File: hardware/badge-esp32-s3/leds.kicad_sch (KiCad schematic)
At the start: 2 parts

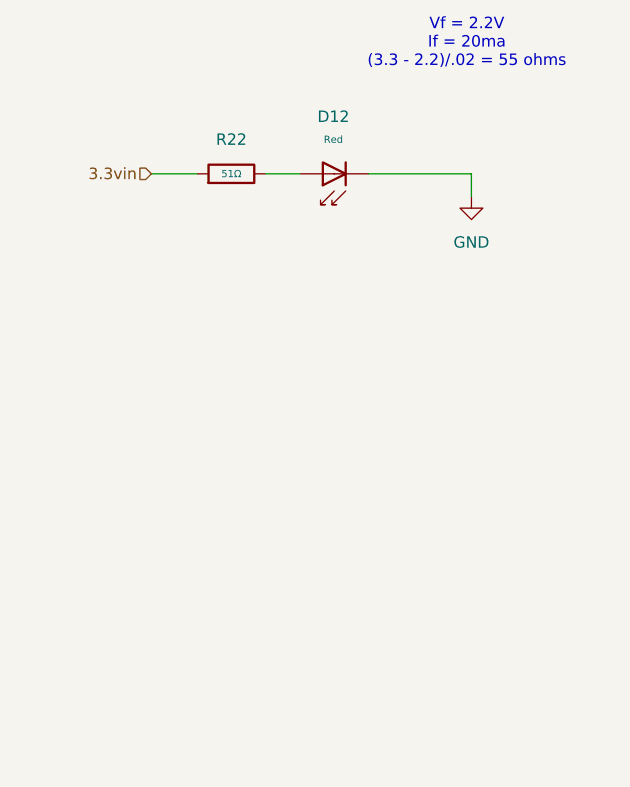
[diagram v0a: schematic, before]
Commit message: Add new tri-color LED, library update
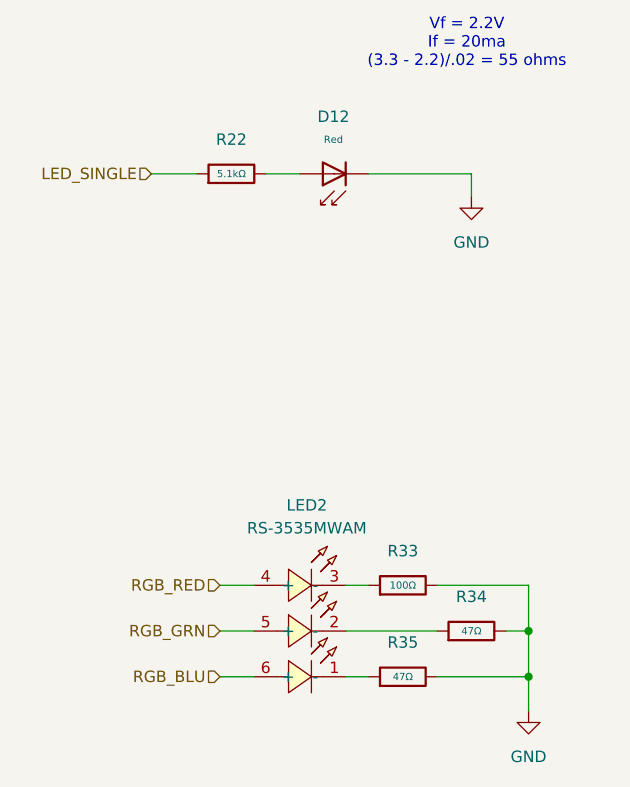
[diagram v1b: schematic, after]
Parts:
- removed R22: 51Ω, PCM_JLCPCB:R_0603, symbol PCM_JLCPCB-Resistors:0603,51Ω
- added LED2: RS-3535MWAM, lcsc-lib:LED-ARRAY-SMD_L3.7-W3.5-P1.10-TL, symbol lcsc-lib:RS-3535MWAM
- added R22: 5.1kΩ, PCM_JLCPCB:R_0402, symbol PCM_JLCPCB-Resistors:0402,5.1kΩ
- added R33: 100Ω, PCM_JLCPCB:R_0402, symbol PCM_JLCPCB-Resistors:0402,100Ω
- added R34, R35: 47Ω, PCM_JLCPCB:R_0402, symbol PCM_JLCPCB-Resistors:0402,47Ω
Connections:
- net GND: now also R33.2, R34.2, R35.2
- net at D12.2: now also R22.2
- new net: LED2.1 (-), R35.1
- new net: LED2.2 (-), R34.1
- new net: LED2.3 (-), R33.1
- new net LED_SINGLE: R22.1
- new net RGB_BLU: LED2.6 (+)
- new net RGB_GRN: LED2.5 (+)
- new net RGB_RED: LED2.4 (+)

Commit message: Annotate schematic
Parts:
- renumbered D12 to D10, LED2 to LED1, R22 to R19, R33 to R20, R35 to R21, R34 to R22
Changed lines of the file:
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@@
 		(dnp no)
 		(fields_autoplaced yes)
-		(property "Reference" "D12"
+		(property "Reference" "D10"
 			(at 135.7947 93.98 90)
 			(effects
@@
 			(project ""
 				(path "/e2af9a6c-dbe9-4de2-9ba6-ea213a7300ec/cf4b41f4-37f8-453c-b748-b2fe0c3fb5a0"
-					(reference "D12")
+					(reference "D10")
 					(unit 1)
 				)
@@
 		(dnp no)
 		(fields_autoplaced yes)
-		(property "Reference" "LED2"
+		(property "Reference" "LED1"
 			(at 132.84 137.16 0)
 			(effects
@@
 			(project ""
 				(path "/e2af9a6c-dbe9-4de2-9ba6-ea213a7300ec/cf4b41f4-37f8-453c-b748-b2fe0c3fb5a0"
-					(reference "LED2")
+					(reference "LED1")
 					(unit 1)
 				)
@@
 		(dnp no)
 		(fields_autoplaced yes)
-		(property "Reference" "R33"
+		(property "Reference" "R20"
 			(at 143.51 142.24 90)
 			(effects
@@
 			(project ""
 				(path "/e2af9a6c-dbe9-4de2-9ba6-ea213a7300ec/cf4b41f4-37f8-453c-b748-b2fe0c3fb5a0"
-					(reference "R33")
+					(reference "R20")
 					(unit 1)
 				)
@@
 		(dnp no)
 		(fields_autoplaced yes)
-		(property "Reference" "R35"
+		(property "Reference" "R21"
 			(at 143.51 152.4 90)
 			(effects
@@
 			(project ""
 				(path "/e2af9a6c-dbe9-4de2-9ba6-ea213a7300ec/cf4b41f4-37f8-453c-b748-b2fe0c3fb5a0"
-					(reference "R35")
+					(reference "R21")
 					(unit 1)
 				)
@@
 		(dnp no)
 		(fields_autoplaced yes)
-		(property "Reference" "#PWR035"
+		(property "Reference" "#PWR032"
 			(at 151.13 109.22 0)
 			(effects
@@
 			(project ""
 				(path "/e2af9a6c-dbe9-4de2-9ba6-ea213a7300ec/cf4b41f4-37f8-453c-b748-b2fe0c3fb5a0"
-					(reference "#PWR035")
+					(reference "#PWR032")
 					(unit 1)
 				)
@@
 		(dnp no)
 		(fields_autoplaced yes)
-		(property "Reference" "#PWR016"
+		(property "Reference" "#PWR033"
 			(at 157.48 166.37 0)
 			(effects
@@
 			(project ""
 				(path "/e2af9a6c-dbe9-4de2-9ba6-ea213a7300ec/cf4b41f4-37f8-453c-b748-b2fe0c3fb5a0"
-					(reference "#PWR016")
+					(reference "#PWR033")
 					(unit 1)
 				)
@@
 		(dnp no)
 		(fields_autoplaced yes)
-		(property "Reference" "R22"
+		(property "Reference" "R19"
 			(at 124.46 96.52 90)
 			(effects
@@
 			(project ""
 				(path "/e2af9a6c-dbe9-4de2-9ba6-ea213a7300ec/cf4b41f4-37f8-453c-b748-b2fe0c3fb5a0"
-					(reference "R22")
+					(reference "R19")
 					(unit 1)
 				)
@@
 		(dnp no)
 		(fields_autoplaced yes)
-		(property "Reference" "R34"
+		(property "Reference" "R22"
 			(at 151.13 147.32 90)
 			(effects
@@
 			(project ""
 				(path "/e2af9a6c-dbe9-4de2-9ba6-ea213a7300ec/cf4b41f4-37f8-453c-b748-b2fe0c3fb5a0"
-					(reference "R34")
+					(reference "R22")
 					(unit 1)
 				)

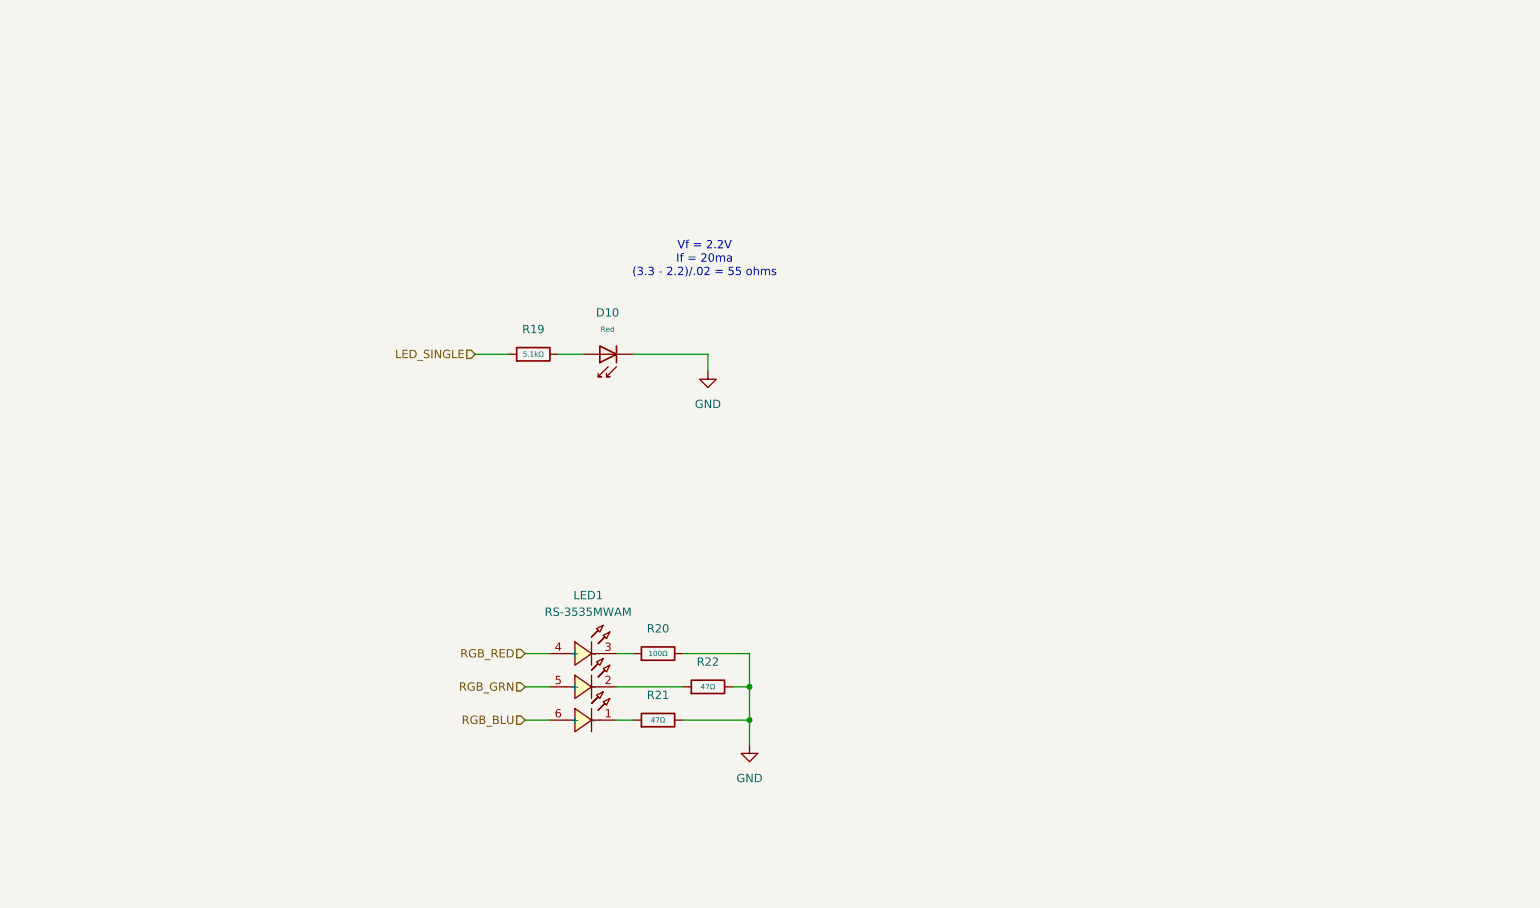
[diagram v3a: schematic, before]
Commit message: Consolidated the GPIO pins, communication pins, and power pins.
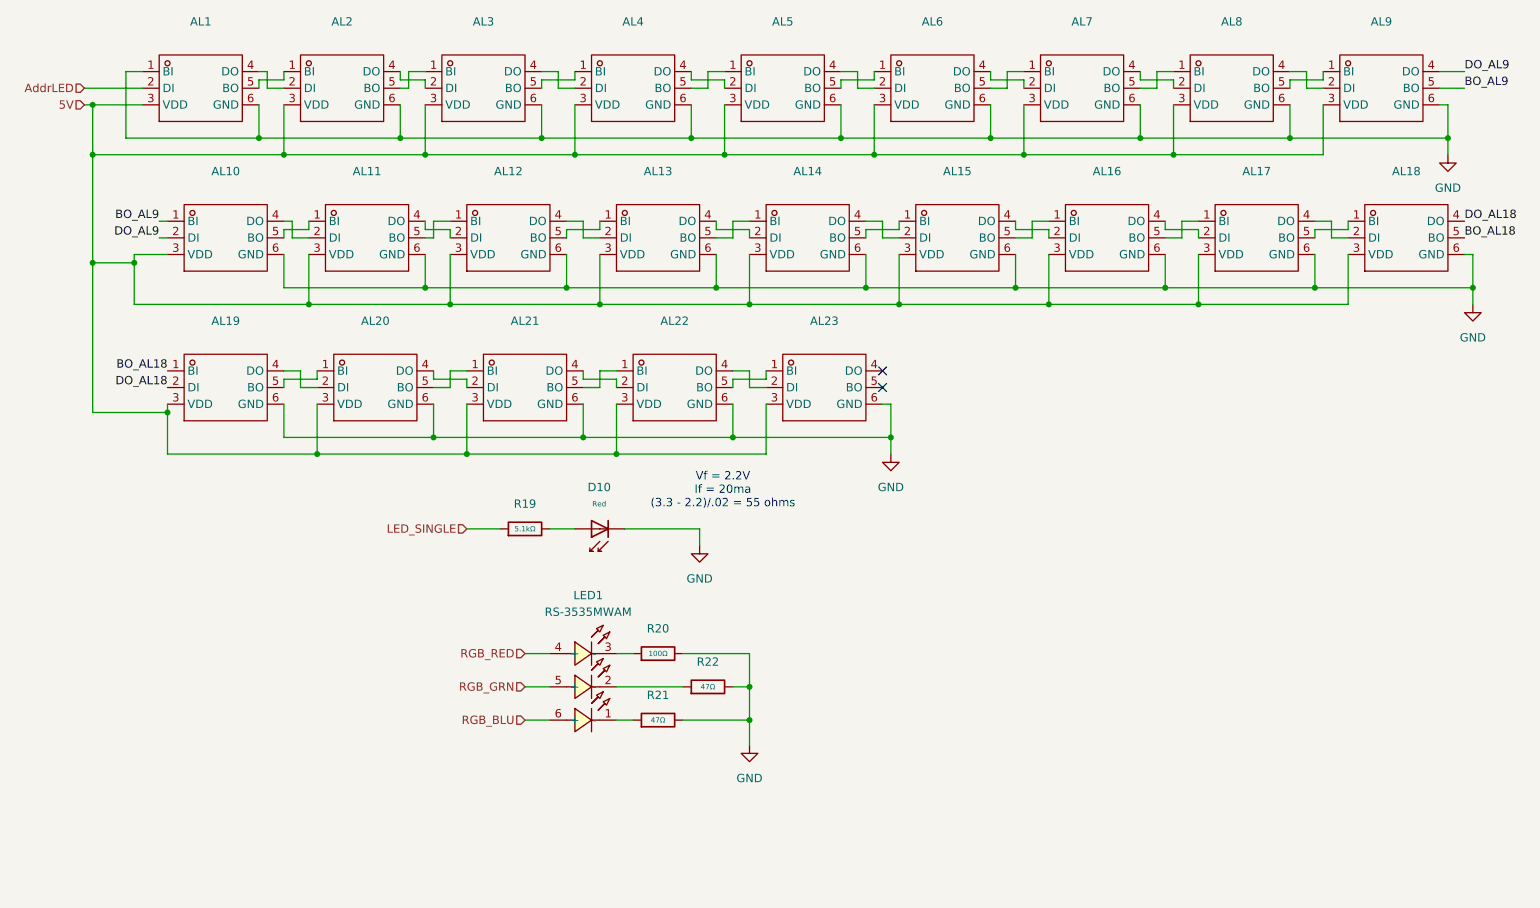
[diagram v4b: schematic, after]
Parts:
- added AL1, AL10, AL11, AL12, AL13, AL14, AL15, AL16, AL17, AL18, AL19, AL2, AL20, AL21, AL22, AL23, AL3, AL4, AL5, AL6, AL7, AL8, AL9: ~, lcsc-lib:LED-SMD_6P-L2.2-W2.2-TL-1, symbol lcsc-lib:WS2813B-2121
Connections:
- net GND: now also AL1.1 (BI), AL1.6 (GND), AL10.6 (GND), AL11.6 (GND), AL12.6 (GND), AL13.6 (GND), AL14.6 (GND), AL15.6 (GND), AL16.6 (GND), AL17.6 (GND), AL18.6 (GND), AL19.6 (GND), AL2.6 (GND), AL20.6 (GND), AL21.6 (GND), AL22.6 (GND), AL23.6 (GND), AL3.6 (GND), AL4.6 (GND), AL5.6 (GND), AL6.6 (GND), AL7.6 (GND), AL8.6 (GND), AL9.6 (GND)
- new net: AL7.5 (BO), AL8.1 (BI)
- new net: AL7.4 (DO), AL8.2 (DI)
- new net: AL8.4 (DO), AL9.2 (DI)
- new net: AL8.5 (BO), AL9.1 (BI)
- new net: AL6.5 (BO), AL7.1 (BI)
- new net: AL6.4 (DO), AL7.2 (DI)
- new net: AL1.5 (BO), AL2.1 (BI)
- new net: AL1.4 (DO), AL2.2 (DI)
- new net: AL2.4 (DO), AL3.2 (DI)
- new net: AL2.5 (BO), AL3.1 (BI)
- new net: AL13.5 (BO), AL14.1 (BI)
- new net: AL13.4 (DO), AL14.2 (DI)
- new net: AL14.4 (DO), AL15.2 (DI)
- new net: AL14.5 (BO), AL15.1 (BI)
- new net: AL19.5 (BO), AL20.1 (BI)
- new net: AL19.4 (DO), AL20.2 (DI)
- new net: AL20.4 (DO), AL21.2 (DI)
- new net: AL20.5 (BO), AL21.1 (BI)
- new net: AL10.4 (DO), AL11.2 (DI)
- new net: AL10.5 (BO), AL11.1 (BI)
- new net: AL3.5 (BO), AL4.1 (BI)
- new net: AL3.4 (DO), AL4.2 (DI)
- new net: AL4.4 (DO), AL5.2 (DI)
- new net: AL4.5 (BO), AL5.1 (BI)
- new net: AL5.4 (DO), AL6.2 (DI)
- new net: AL5.5 (BO), AL6.1 (BI)
- new net: AL12.5 (BO), AL13.1 (BI)
- new net: AL12.4 (DO), AL13.2 (DI)
- new net: AL15.5 (BO), AL16.1 (BI)
- new net: AL15.4 (DO), AL16.2 (DI)
- new net: AL16.4 (DO), AL17.2 (DI)
- new net: AL16.5 (BO), AL17.1 (BI)
- new net: AL11.4 (DO), AL12.2 (DI)
- new net: AL11.5 (BO), AL12.1 (BI)
- new net: AL21.5 (BO), AL22.1 (BI)
- new net: AL21.4 (DO), AL22.2 (DI)
- new net: AL22.4 (DO), AL23.2 (DI)
- new net: AL22.5 (BO), AL23.1 (BI)
- new net: AL17.4 (DO), AL18.2 (DI)
- new net: AL17.5 (BO), AL18.1 (BI)
- new net 5V: AL1.3 (VDD), AL10.3 (VDD), AL11.3 (VDD), AL12.3 (VDD), AL13.3 (VDD), AL14.3 (VDD), AL15.3 (VDD), AL16.3 (VDD), AL17.3 (VDD), AL18.3 (VDD), AL19.3 (VDD), AL2.3 (VDD), AL20.3 (VDD), AL21.3 (VDD), AL22.3 (VDD), AL23.3 (VDD), AL3.3 (VDD), AL4.3 (VDD), AL5.3 (VDD), AL6.3 (VDD), AL7.3 (VDD), AL8.3 (VDD), AL9.3 (VDD)
- new net AddrLED: AL1.2 (DI)
- new net BO_AL18: AL18.5 (BO), AL19.1 (BI)
- new net BO_AL9: AL10.1 (BI), AL9.5 (BO)
- new net DO_AL18: AL18.4 (DO), AL19.2 (DI)
- new net DO_AL9: AL10.2 (DI), AL9.4 (DO)
- no-connect marks 0 -> 2
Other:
- moved on the sheet: D10, R19

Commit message: almost finished
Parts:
- removed D10: Red, PCM_JLCPCB:D_0603, symbol PCM_JLCPCB-Diodes:LED,0603,Red
- added AL24: ~, lcsc-lib:LED-SMD_6P-L2.2-W2.2-TL-1, symbol lcsc-lib:WS2813B-2121
- added C32, C33: 1uF, PCM_JLCPCB:C_0402, symbol PCM_JLCPCB-Capacitors:0402,1uF
- added D14: Red, PCM_JLCPCB:D_0603, symbol PCM_JLCPCB-Diodes:LED,0603,Red
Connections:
- net 5V: now also AL24.3 (VDD), C32.1, C33.1
- net GND: now also AL24.6 (GND), C32.2, C33.2, D14.1
- net at R19.2: now also D14.2
- net at AL23.4 (DO): now also AL24.2 (DI)
- net at AL23.5 (BO): now also AL24.1 (BI)
- net LED_SINGLE renamed LED_SINGLE1
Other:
- moved on the sheet: LED1, R20, R21, R22

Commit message: final changes and part updated
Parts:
- AL1, AL10, AL11, AL12, AL13, AL14, AL15, AL16, AL17, AL18, AL19, AL2, AL20, AL21, AL22, AL23, AL24, AL3, AL4, AL5, AL6, AL7, AL8, AL9: LCSC (none) -> C22371528; Supplier Part C22371528 -> (none)
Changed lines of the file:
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@@
 			)
 		)
-		(property "Supplier Part" "C22371528"
+		(property "LCSC" "C22371528"
 			(at 231.14 59.69 0)
 			(effects
@@
 			)
 		)
-		(property "Supplier Part" "C22371528"
+		(property "LCSC" "C22371528"
 			(at 208.28 59.69 0)
 			(effects
@@
 			)
 		)
-		(property "Supplier Part" "C22371528"
+		(property "LCSC" "C22371528"
 			(at 95.25 59.69 0)
 			(effects
@@
 			)
 		)
-		(property "Supplier Part" "C22371528"
+		(property "LCSC" "C22371528"
 			(at 166.37 82.55 0)
 			(effects
@@
 			)
 		)
-		(property "Supplier Part" "C22371528"
+		(property "LCSC" "C22371528"
 			(at 100.33 105.41 0)
 			(effects
@@
 			)
 		)
-		(property "Supplier Part" "C22371528"
+		(property "LCSC" "C22371528"
 			(at 77.47 82.55 0)
 			(effects
@@
 			)
 		)
-		(property "Supplier Part" "C22371528"
+		(property "LCSC" "C22371528"
 			(at 139.7 59.69 0)
 			(effects
@@
 			)
 		)
-		(property "Supplier Part" "C22371528"
+		(property "LCSC" "C22371528"
 			(at 162.56 59.69 0)
 			(effects
@@
 			)
 		)
-		(property "Supplier Part" "C22371528"
+		(property "LCSC" "C22371528"
 			(at 143.51 82.55 0)
 			(effects
@@
 			)
 		)
-		(property "Supplier Part" "C22371528"
+		(property "LCSC" "C22371528"
 			(at 212.09 82.55 0)
 			(effects
@@
 			)
 		)
-		(property "Supplier Part" "C22371528"
+		(property "LCSC" "C22371528"
 			(at 73.66 59.69 0)
 			(effects
@@
 			)
 		)
-		(property "Supplier Part" "C22371528"
+		(property "LCSC" "C22371528"
 			(at 99.06 82.55 0)
 			(effects
@@
 			)
 		)
-		(property "Supplier Part" "C22371528"
+		(property "LCSC" "C22371528"
 			(at 120.65 82.55 0)
 			(effects
@@
 			)
 		)
-		(property "Supplier Part" "C22371528"
+		(property "LCSC" "C22371528"
 			(at 116.84 59.69 0)
 			(effects
@@
 			)
 		)
-		(property "Supplier Part" "C22371528"
+		(property "LCSC" "C22371528"
 			(at 185.42 59.69 0)
 			(effects
@@
 			)
 		)
-		(property "Supplier Part" "C22371528"
+		(property "LCSC" "C22371528"
 			(at 191.77 105.41 0)
 			(effects
@@
 			)
 		)
-		(property "Supplier Part" "C22371528"
+		(property "LCSC" "C22371528"
 			(at 189.23 82.55 0)
 			(effects
@@
 			)
 		)
-		(property "Supplier Part" "C22371528"
+		(property "LCSC" "C22371528"
 			(at 146.05 105.41 0)
 			(effects
@@
 			)
 		)
-		(property "Supplier Part" "C22371528"
+		(property "LCSC" "C22371528"
 			(at 254 59.69 0)
 			(effects
@@
 			)
 		)
-		(property "Supplier Part" "C22371528"
+		(property "LCSC" "C22371528"
 			(at 123.19 105.41 0)
 			(effects
@@
 			)
 		)
-		(property "Supplier Part" "C22371528"
+		(property "LCSC" "C22371528"
 			(at 234.95 82.55 0)
 			(effects
@@
 			)
 		)
-		(property "Supplier Part" "C22371528"
+		(property "LCSC" "C22371528"
 			(at 257.81 82.55 0)
 			(effects
@@
 			)
 		)
-		(property "Supplier Part" "C22371528"
+		(property "LCSC" "C22371528"
 			(at 77.47 105.41 0)
 			(effects
@@
 			)
 		)
-		(property "Supplier Part" "C22371528"
+		(property "LCSC" "C22371528"
 			(at 168.91 105.41 0)
 			(effects
